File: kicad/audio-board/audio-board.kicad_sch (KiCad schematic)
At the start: 117 parts, among them J1 HOST_J3 (AeroNode), J2 HOST_J4 (AeroNode), J3 CUP_L (A2B + speaker), J4 CUP_R (speaker), J5 PANEL (ear + mic), J6 FAILSAFE_ELECTRET, Q1 AO3401A, Q2 2N7002, T2 Triad SP-74 (cup L), T3 Triad SP-74 (cup R), T4 Bourns SM-LP-5001 (600:600), U1 TPS62162DSG, U10 AQW612S (K1 mic-hi), U11 AQW612S (K1 mic-lo), U12 LM2731XMF (8 V A2B bus), U2 TPS62160DSG, U3 ADP7118AUJZ-3.3-R7, U4 ADAU1467, U5 W25Q32JVSS, U6 ADAU1372, U7 IM68A130A, U9 AD2428WBCPZ, Y1 SiT8008 12.288MHz 3.3V

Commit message: [LIMA] audio board: all 121 parts placed (117 + 4 holes), placement DRC-clean
Synced from the schematic (one KiCad undo step), then placed by block:
host J1/J2 top edge, power top-left, hub centre with decoupling ring,
codec below-right, A2B node + bus filter + J3/J4 on the right edge,
K1 PhotoMOS by J5/J6 on the left edge, T2/T3/T4 along the bottom.
Placement table checked against real courtyards before applying.

Mounting holes H1-H4 now live in the schematic (Mechanical:MountingHole),
so future syncs don't trip on blank-identity board-only footprints.
Rules: min hole 0.2 (JLC 4-layer allows 0.15/0.25 via), Default and Power
clearance 0.127 (LFCSP corner pads sit 0.148 apart).

Checked on the saved file: DRC errors = 326 unconnected only; netlist ==
design file; ERC 0 errors. Not yet routed.

Co-Authored-By: Claude Opus 5.5 <noreply@anthropic.com>
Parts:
- added H1, H2, H3, H4: M3, MountingHole:MountingHole_3.2mm_M3, symbol Mechanical:MountingHole

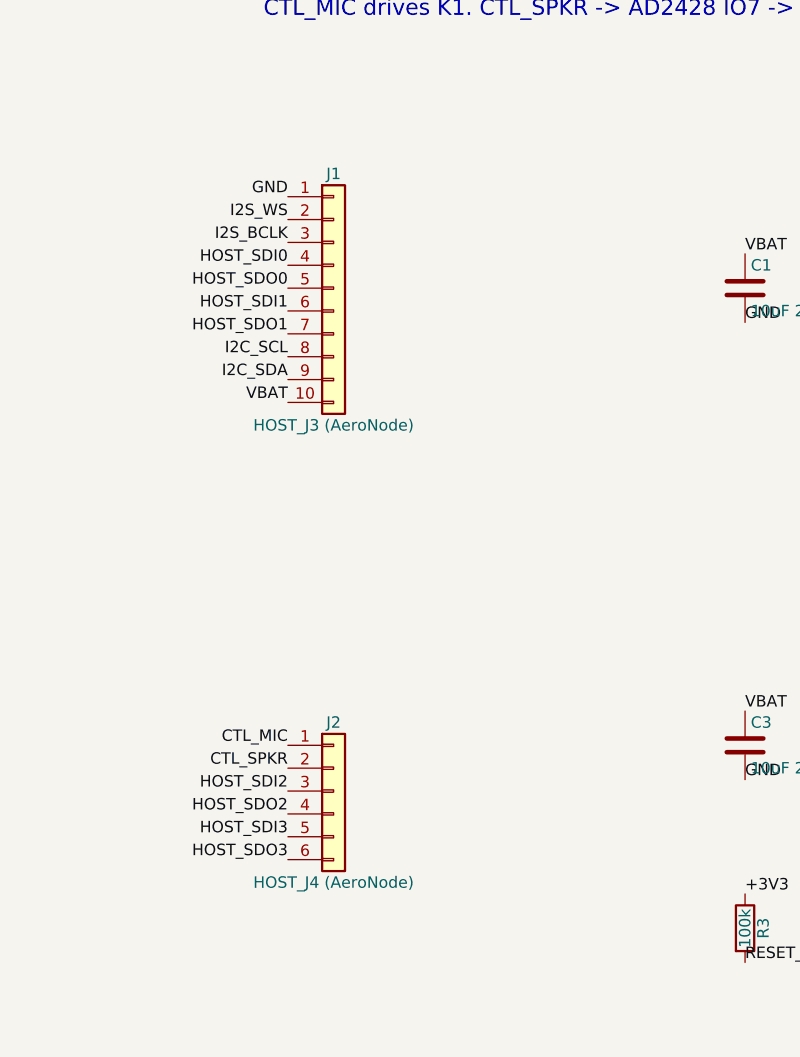
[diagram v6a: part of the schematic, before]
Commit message: [LIMA] audio board: J1+J2 -> one 24-pin FFC mating AeroNode J9
Peter 2026-10-26: one flat-flex connector instead of J1/J2. AeroNode HW 0.0.2
rev 1 sheet 6 already has J9 "audio breakout", Cvilux CF31241D0R0-05-NH (0.5 mm,
bottom contact). Ours is the same part; flat cable, connectors facing, Type A
FFC -> our pin n = J9 pin 25-n (Peter chose the route). 8 GND contacts incl.
shell; J9.2 Vcm3.3 and J9.16 reserved left NC.

New footprint Cvilux_CF31241D0R0-05-NH from drawing CF3101SF sheet 2
(tab-pad x derived from C/F - flagged). Checked: netlist == design_nets.py,
J9 pin-by-pin cross-check 0 mismatches, ERC 0 errors. PCB not yet synced.

Flagged for the AeroNode owner: board power is one contact behind a
100 mA-hold polyfuse; this board needs ~0.35 A typ / 0.5 A worst.

Co-Authored-By: Claude Opus 5.5 <noreply@anthropic.com>
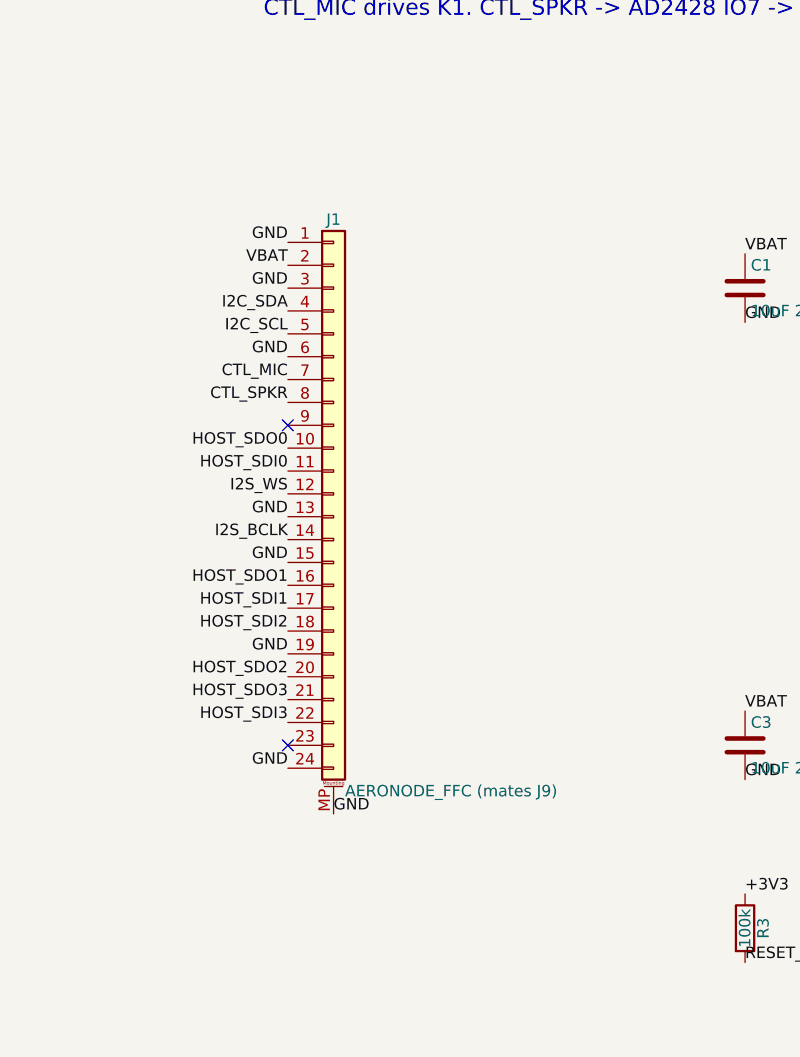
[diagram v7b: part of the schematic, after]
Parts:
- removed J1: HOST_J3 (AeroNode), Connector_JST:JST_GH_SM10B-GHS-TB_1x10-1MP_P1.25mm_Horizontal, symbol Connector_Generic:Conn_01x10
- removed J2: HOST_J4 (AeroNode), Connector_JST:JST_GH_SM06B-GHS-TB_1x06-1MP_P1.25mm_Horizontal, symbol Connector_Generic:Conn_01x06
- added J1: AERONODE_FFC (mates J9), Cvilux:Cvilux_CF31241D0R0-05-NH_1x24-1MP_P0.5mm_Horizontal, symbol Connector_Generic_MountingPin:Conn_01x24_MountingPin
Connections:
- net CTL_MIC: now also J1.7 (Pin_7)
- net CTL_SPKR: now also J1.8 (Pin_8)
- net GND: now also J1.1 (Pin_1), J1.13 (Pin_13), J1.15 (Pin_15), J1.19 (Pin_19), J1.24 (Pin_24), J1.3 (Pin_3), J1.6 (Pin_6), J1.MP (MountPin)
- net HOST_SDI0: now also J1.11 (Pin_11)
- net HOST_SDI1: now also J1.17 (Pin_17)
- net HOST_SDI2: now also J1.18 (Pin_18)
- net HOST_SDI3: now also J1.22 (Pin_22)
- net HOST_SDO0: now also J1.10 (Pin_10)
- net HOST_SDO1: now also J1.16 (Pin_16)
- net HOST_SDO2: now also J1.20 (Pin_20)
- net HOST_SDO3: now also J1.21 (Pin_21)
- net I2C_SCL: now also J1.5 (Pin_5)
- net I2C_SDA: now also J1.4 (Pin_4)
- net I2S_BCLK: now also J1.14 (Pin_14)
- net I2S_WS: now also J1.12 (Pin_12)
- net VBAT: now also J1.2 (Pin_2)
- no-connect marks 42 -> 44

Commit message: [LIMA] schematics: boom electret pass-through via the cups (Peter)
Cup: J12 2-pin boom electret in -> J7.5/J7.6 (J7 now 6-pin SM06B). ELEC_HI/ELEC_LO touch nothing else on the cup.
Audio: J3 6-pin (5/6 = ELEC_HI/LO from cup L), J4 4-pin (3/4 = ELEC_HI/LO from cup R), joined to the existing J6/K1 nets.
Netlist == design files on both; ERC warnings unchanged (pin-type only).

Co-Authored-By: Claude Opus 5.5 <noreply@anthropic.com>
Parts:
- J3: value CUP_L (A2B + speaker) -> CUP_L (A2B + speaker + boom electret); footprint Connector_JST:JST_GH_SM04B-GHS-TB_1x04-1MP_P1.25mm_Horizontal -> Connector_JST:JST_GH_SM06B-GHS-TB_1x06-1MP_P1.25mm_Horizontal; symbol Connector_Generic:Conn_01x04 -> Connector_Generic:Conn_01x06
- J4: value CUP_R (speaker) -> CUP_R (speaker + boom electret); footprint Connector_JST:JST_GH_SM02B-GHS-TB_1x02-1MP_P1.25mm_Horizontal -> Connector_JST:JST_GH_SM04B-GHS-TB_1x04-1MP_P1.25mm_Horizontal; symbol Connector_Generic:Conn_01x02 -> Connector_Generic:Conn_01x04
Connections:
- net ELEC_HI: now also J3.5 (Pin_5), J4.3 (Pin_3)
- net ELEC_LO: now also J3.6 (Pin_6), J4.4 (Pin_4)
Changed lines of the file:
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@@
 		(at 25.4 114.3)
 	)
+	(wire
+		(pts
+			(xy 779.78 485.14)
+			(xy 777.24 485.14)
+		)
+	)
+	(wire
+		(pts
+			(xy 779.78 487.68)
+			(xy 777.24 487.68)
+		)
+	)
+	(wire
+		(pts
+			(xy 248.92 477.52)
+			(xy 246.38 477.52)
+		)
+	)
+	(wire
+		(pts
+			(xy 248.92 480.06)
+			(xy 246.38 480.06)
+		)
+	)
 	(text "HUB: ADAU1467 (clock master, routing, CM5 I/O)\nOne 12.288 MHz XO into XTALIN/MCLK; hub drives CODEC_MCLK (CLKOUT) and every BCLK/LRCLK.\nSelf-boot from U5 W25Q32 on the SPI master (SPI mode 3, read 0x03). I2C slave, ADDR1/ADDR0 = 0.\nPLL filter per DS Fig. 16 (150 pF || 5.6 nF + 4.3 k, to PVDD). VDRIVE to GND via R26: DVDD is external.\nOUT0/IN0 = CM5, OUT2/IN2 = codec, OUT3/IN3 + SDATAIO4/5 = A2B, SDATAIO0-3 = spare CM5 lanes.\nThe coefficient channel must be routed bit-exact: no ASRC, gain, mix or dither."
 		(at 365.76 93.98 0)
@@
 		)
 	)
+	(label "ELEC_HI"
+		(at 777.24 485.14 180)
+		(effects
+			(font
+				(size 1.27 1.27)
+			)
+			(justify right bottom)
+		)
+	)
+	(label "ELEC_LO"
+		(at 777.24 487.68 180)
+		(effects
+			(font
+				(size 1.27 1.27)
+			)
+			(justify right bottom)
+		)
+	)
+	(label "ELEC_HI"
+		(at 246.38 477.52 180)
+		(effects
+			(font
+				(size 1.27 1.27)
+			)
+			(justify right bottom)
+		)
+	)
+	(label "ELEC_LO"
+		(at 246.38 480.06 180)
+		(effects
+			(font
+				(size 1.27 1.27)
+			)
+			(justify right bottom)
+		)
+	)
 	(symbol
 		(lib_id "Regulator_Switching:TPS62162DSG")
@@
 	)
 	(symbol
-		(lib_id "Connector_Generic:Conn_01x04")
-		(at 784.86 477.52 0)
+		(lib_id "Connector_Generic:Conn_01x06")
+		(at 784.86 480.06 0)
 		(unit 1)
 		(in_bom yes)
@@
 		(dnp no)
 		(property "Reference" "J3"
-			(at 784.86 472.44 0)
+			(at 784.86 474.98 0)
 			(effects
 				(font
@@
 			)
 		)
-		(property "Value" "CUP_L (A2B + speaker)"
-			(at 784.86 485.14 0)
+		(property "Value" "CUP_L (A2B + speaker + boom electret)"
+			(at 784.86 487.68 0)
 			(effects
 				(font
@@
 			)
 		)
-		(property "Footprint" "Connector_JST:JST_GH_SM04B-GHS-TB_1x04-1MP_P1.25mm_Horizontal"
-			(at 784.86 477.52 0)
+		(property "Footprint" "Connector_JST:JST_GH_SM06B-GHS-TB_1x06-1MP_P1.25mm_Horizontal"
+			(at 784.86 480.06 0)
 			(hide yes)
 			(effects
@@
 		)
 		(property "Datasheet" ""
-			(at 784.86 477.52 0)
+			(at 784.86 480.06 0)
 			(hide yes)
 			(effects
@@
 	)
 	(symbol
-		(lib_id "Connector_Generic:Conn_01x02")
-		(at 254 472.44 0)
+		(lib_id "Connector_Generic:Conn_01x04")
+		(at 254 474.98 0)
 		(unit 1)
 		(in_bom yes)
@@
 		(dnp no)
 		(property "Reference" "J4"
-			(at 254 469.9 0)
+			(at 254 472.44 0)
 			(effects
 				(font
@@
 			)
 		)
-		(property "Value" "CUP_R (speaker)"
-			(at 254 477.52 0)
+		(property "Value" "CUP_R (speaker + boom electret)"
+			(at 254 480.06 0)
 			(effects
 				(font
@@
 			)
 		)
-		(property "Footprint" "Connector_JST:JST_GH_SM02B-GHS-TB_1x02-1MP_P1.25mm_Horizontal"
-			(at 254 472.44 0)
+		(property "Footprint" "Connector_JST:JST_GH_SM04B-GHS-TB_1x04-1MP_P1.25mm_Horizontal"
+			(at 254 474.98 0)
 			(hide yes)
 			(effects
@@
 		)
 		(property "Datasheet" ""
-			(at 254 472.44 0)
+			(at 254 474.98 0)
 			(hide yes)
 			(effects
@@
 			)
 		)
-		(instances
-			(project "audio-board"
-				(path "/95b6c2e6-5cb2-4173-9673-0cba23213f90"
-					(reference "J1")
-					(unit 1)
-				)
-			)
-		)
 		(property "Cable" "0.5 mm FFC, 24 cond, Type A (same-side contacts); pin n = AeroNode J9 pin 25-n"
 			(at 30.48 86.36 0)
@@
 				)
 			)
-		))
+		)
+		(instances
+			(project "audio-board"
+				(path "/95b6c2e6-5cb2-4173-9673-0cba23213f90"
+					(reference "J1")
+					(unit 1)
+				)
+			)
+		)
+	)
 )
